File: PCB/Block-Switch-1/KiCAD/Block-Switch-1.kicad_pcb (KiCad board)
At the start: 2 copper layers, 24.1 x 24.1 mm, 8 parts, among them J1 Samtec MTMS-105-02-T-S-100, J2 Samtec MTMS-104-02-T-S-100, J3 Samtec MTMS-106-02-T-S-100, J4 Samtec MTMS-104-02-T-S-100, SW1 SW_Push

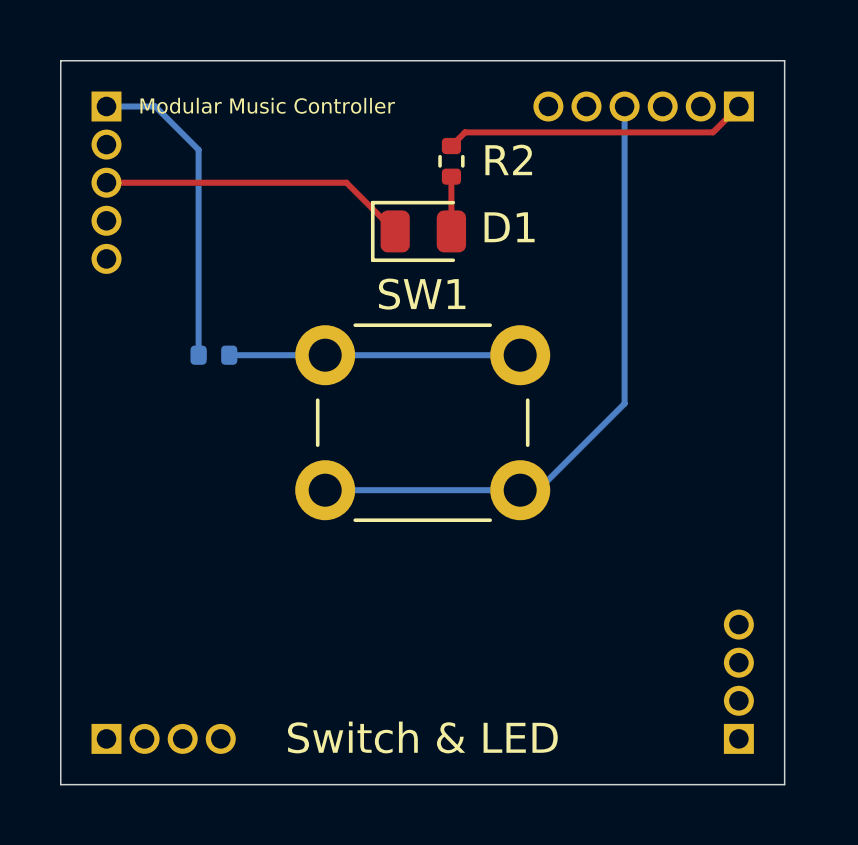
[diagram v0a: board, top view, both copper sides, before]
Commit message: PCBs for different blocks
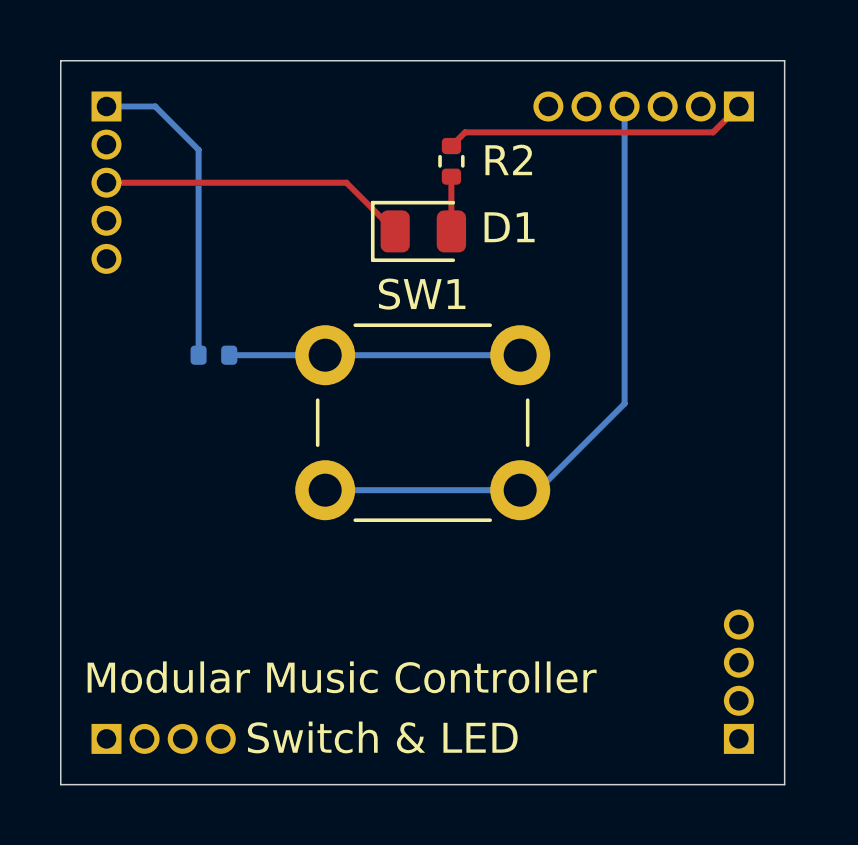
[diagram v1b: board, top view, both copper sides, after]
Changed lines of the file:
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@@
 	)
 	(paper "A4")
+	(title_block
+		(title "Modular Music Controller / Block / One Switch")
+		(date "2025-12-03")
+		(rev "1")
+	)
 	(layers
 		(0 "F.Cu" signal)
@@
 			(crossoutdnponfab yes)
 			(subtractmaskfromsilk no)
-			(outputformat 4)
+			(outputformat 1)
 			(mirror no)
 			(drillshape 0)
 			(scaleselection 1)
-			(outputdirectory "../PDF/PCB Layers/")
+			(outputdirectory "../Gerber/")
 		)
 	)
@@
 	)
 	(gr_text "Switch & LED"
-		(at 139.065 124.206 0)
+		(at 133.1468 124.205 0)
 		(layer "F.SilkS")
 		(effects
@@
 				(thickness 0.125)
 			)
+			(justify left)
 		)
 	)
 	(gr_text "Modular Music Controller"
-		(at 129.5908 103.125 0)
+		(at 127.762 121.6152 0)
 		(layer "F.SilkS")
 		(effects
 			(font
-				(size 0.5 0.5)
-				(thickness 0.0625)
-			)
-			(justify left)
+				(size 1 1)
+				(thickness 0.125)
+			)
+			(justify left top)
 		)
 	)
